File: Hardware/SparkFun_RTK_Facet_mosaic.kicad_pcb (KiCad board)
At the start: 4 copper layers, 59.5 x 43 mm, 128 parts, among them J1 U.FL_SMD, J2 JST_2mm_LiPo, J3 Qwiic_RA, J5 Conn_01x12_FPC_0.5mm, J6 Conn_01x12_FPC_0.5mm, J7 Conn_01x12_FPC_0.5mm, Q1 MBT3904DW1, Q2 SIL2308, U1 ESP32-PICO-V3-02, U10 MCP73833_MSOP, U11 AP2112K-3.3, U12 STLQ015-3.3, U13 74HC4052D, U2 mosaic-X5, U3 CH340C, U4 MAX17048, U5 AP2112K-3.3, U6 Power_Divider, U8 NEO-D9S, U9 USB251xB, Y1 24MHz

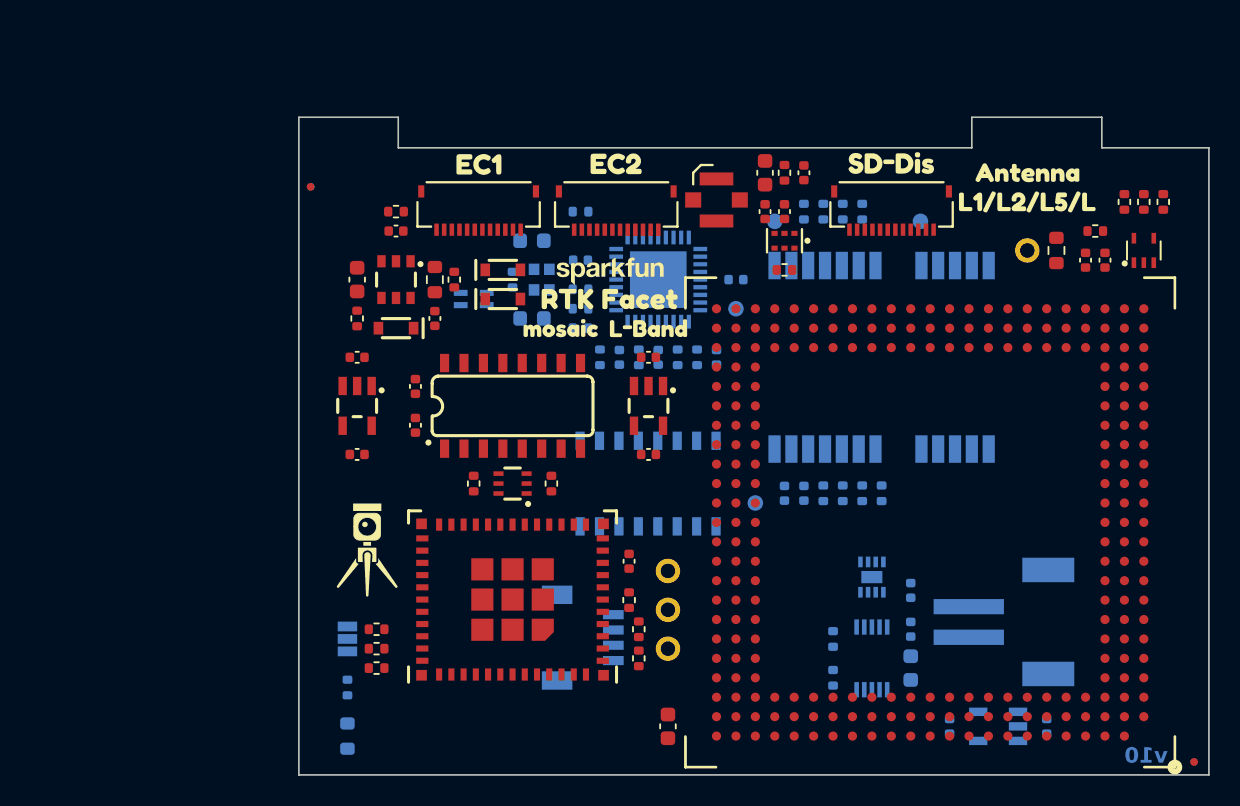
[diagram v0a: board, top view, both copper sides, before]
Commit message: Schematic updates
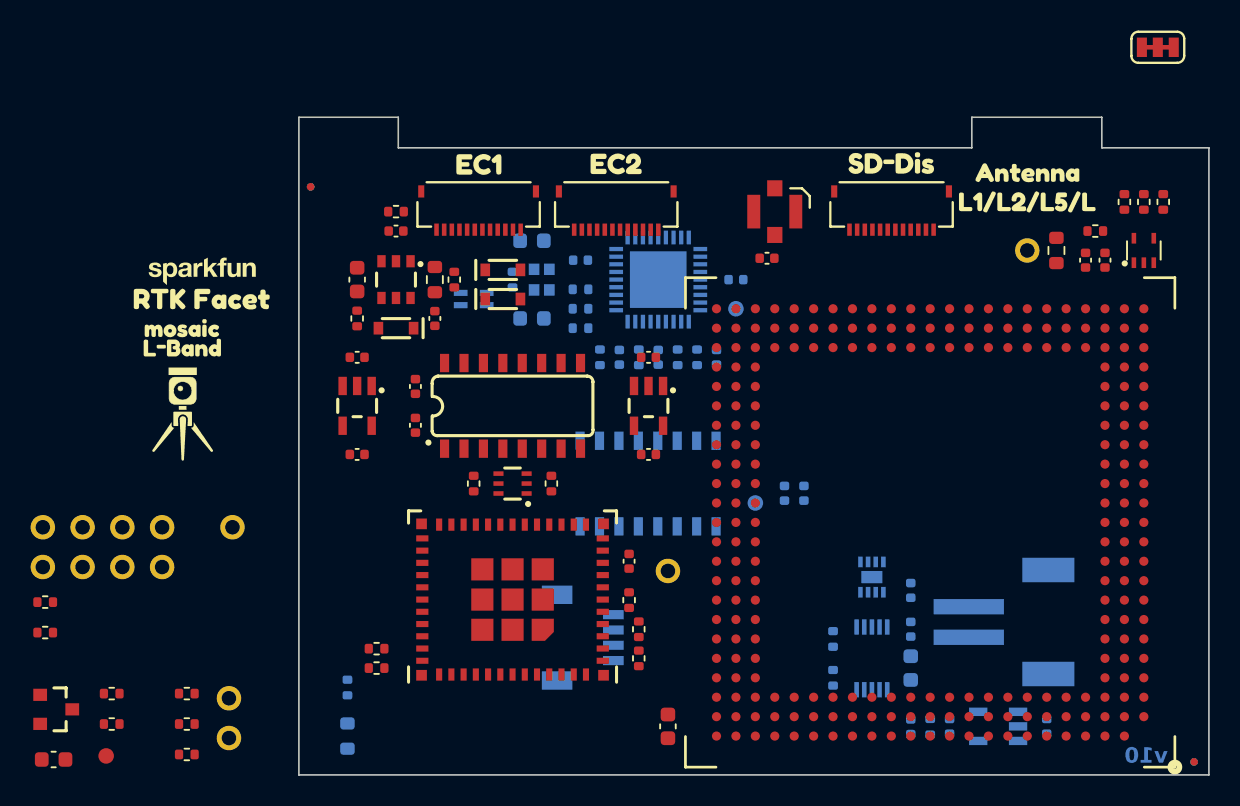
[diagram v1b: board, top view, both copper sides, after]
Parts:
- removed C9: 47pF, SparkFun-Capacitor:C_0402_1005Metric
- removed R18: 33, SparkFun-Resistor:R_0402_1005Metric
- removed R22: 100k, SparkFun-Resistor:R_0402_1005Metric
- removed R39, R40: 27, SparkFun-Resistor:R_0402_1005Metric
- removed U6: Power_Divider, SparkFun-RF:PD0922J5050S2HF_ANA
- removed U8: NEO-D9S, SparkFun-GPS:NEO-M9N_M8T_M8U_D9S_F9P_F10N
- added Q3: BSS138, SparkFun-Semiconductor-Standard:SOT23-3, F.Cu at (85.7, 148.1)
- added TP10: PTH, SparkFun-Connector:1X01, F.Cu at (90.1, 138.8)
- added TP11: PTH, SparkFun-Connector:1X01, F.Cu at (92.7, 136.2)
- added TP12: PTH, SparkFun-Connector:1X01, F.Cu at (92.7, 138.8)
- added TP13: PTH, SparkFun-Connector:1X01, F.Cu at (97.3, 136.2)
- added TP14: 1.0mm, SparkFun-Connector:TestPoint-1.0mm, F.Cu at (89.0, 151.2)
- added TP15: PTH, SparkFun-Connector:1X01, F.Cu at (97.0, 147.4)
- added TP16: PTH, SparkFun-Connector:1X01, F.Cu at (97.0, 150.0)
- added TP9: PTH, SparkFun-Connector:1X01, F.Cu at (90.1, 136.2)
- C3: value 47pF -> 0.1uF; moved to B.Cu
- JP1: footprint SparkFun-Jumper:SMT-JUMPER_3_NO_SILK -> SparkFun-Jumper:SMT-JUMPER_3_2-NC_TRACE_SILK; moved to F.Cu
- L1: value 2.66Ohm -> 470Ohm
- R10, R9: value 33 -> 10k; moved to F.Cu
- R11: value 10 -> 10k; moved to B.Cu
- R12: value 100 -> 2.2k
- R13: value 33 -> 2.2k; moved to F.Cu
- R14, R15: value 33 -> 100k; moved to F.Cu
- R17: value 10k -> 12k
- TP1, TP4: value 1.0mm -> PTH; footprint SparkFun-Connector:TestPoint-1.0mm -> SparkFun-Connector:1X01; moved to F.Cu
- moved JP1 65.6 mm to (157.8, 104.8), turned to 0 degrees
- moved TP1 60.8 mm to (84.9, 136.2), turned to 0 degrees
- moved L1 60.3 mm to (85.6, 151.4), turned to 0 degrees
- moved R13 56.3 mm to (89.4, 149.1), turned to 0 degrees
- moved R9 55.1 mm to (85.0, 141.1), turned to 0 degrees
- moved R10 54.2 mm to (85.0, 143.1), turned to 0 degrees
- moved TP4 52.9 mm to (84.9, 138.8)
- moved R14 52.2 mm to (94.3, 147.1), turned to 0 degrees
- moved R12 52.0 mm to (89.4, 147.1)
- moved R15 45.5 mm to (94.3, 149.1), turned to 0 degrees
- moved TP7 38.7 mm to (87.5, 136.2)
- moved TP8 38.6 mm to (87.5, 138.8)
- moved R11 37.5 mm to (142.9, 149.3)
- moved C3 36.9 mm to (141.6, 149.3), turned to 90 degrees
- moved kibuzzard-65777033 30.5 mm to (94.0, 124.5)
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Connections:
- C3 pad 1: Net-(C3-Pad1) -> Net-(U2-~{RESET})
- D1 pad 2: Net-(D1-A2) -> MOSAIC_RF_IN
- J1 pad 1: Net-(D1-A2) -> MOSAIC_RF_IN
- J2 pad NC1: (no net) -> unconnected-(J2-PadNC1)
- J2 pad NC2: (no net) -> unconnected-(J2-PadNC2)
- J3 pad 3: ESP8/SDA -> ESP21/SDA
- J3 pad 4: ESP9/SCL -> ESP22/SCL
- J6 pad 3: ESP9/SCL -> ESP22/SCL
- J6 pad 4: ESP8/SDA -> ESP21/SDA
- J7 pad 11: CHG_LED -> ESP34/CHG_LED
- JP1 pad 2: 3.3V_P -> 3.3V
- L1 pad 1: Net-(C3-Pad1) -> VRAW
- L1 pad 2: Net-(D1-A2) -> VANT
- R10 pad 1: Net-(U8-SCL/SCK) -> 3.3V
- R10 pad 2: ESP22/SCL -> ESP34/CHG_LED
- R11 pad 1: Net-(C3-Pad1) -> 3.3V_P
- R11 pad 2: 3.3V_P -> Net-(U2-~{RESET})
- R12 pad 1: MOSAIC_RF_IN -> 1.8V
- R12 pad 2: NEO_RF_IN -> MPPS
- R13 pad 1: Net-(U8-TX2) -> 3.3V_P
- R13 pad 2: ESP4/NEO_TX -> MPPS_3V3
- R14 pad 1: Net-(U8-RX2) -> Net-(U9-SDA)
- R14 pad 2: ESP25/NEO_RX -> GND
- R15 pad 1: Net-(U8-TX1/POCI) -> Net-(U9-SCL/CFG0)
- R15 pad 2: unconnected-(R15-Pad2) -> GND
- R17 pad 1: 3.3V_P -> GND
- R17 pad 2: ESP19/MLOG -> Net-(U9-RBIAS)
- R37 pad 2: SD_CLK -> SD_CMD
- R7 pad 2: ESP36/DeviceSense -> ESP35/DeviceSense
- R8 pad 1: ESP36/DeviceSense -> ESP35/DeviceSense
- R9 pad 1: Net-(U8-SDA/~{CS}) -> 3.3V
- R9 pad 2: ESP21/SDA -> ESP36/CHG_S2
- TP1 pad 1: Net-(U8-~{RESET}) -> 3.3V
- TP4 pad 1: Net-(U8-~{SAFEBOOT}) -> GND
- TP7 pad 1: 3.3V -> 3.3V_P
- TP8 pad 1: GND -> VRAW
- U1 pad 10: ESP35/CHG_S2 -> ESP35/DeviceSense
- U1 pad 15: ESP25/NEO_RX -> ESP25/MRX4
- U1 pad 21: ESP15/M~{RESET} -> unconnected-(U1-IOA15-Pad21)
- U1 pad 24: ESP4/NEO_TX -> ESP4/MTX4
- U1 pad 33: ESP19/MLOG -> unconnected-(U1-IO19-Pad33)
- U1 pad 4: ESP36/DeviceSense -> ESP36/CHG_S2
- U1 pad 5: unconnected-(U1-IA37-Pad5) -> ESP37/MRDY
- U10 pad 4: ESP35/CHG_S2 -> ESP36/CHG_S2
- U13 pad 14: MPPS -> MPPS_3V3
- U13 pad 15: ESP9/SCL -> ESP22/SCL
- U13 pad 2: ESP8/SDA -> ESP21/SDA
- U2 pad A11: ESP15/M~{RESET} -> Net-(U2-~{RESET})
- U2 pad A12: unconnected-(U2-MODULE_RDY-PadA12) -> ESP37/MRDY
- U2 pad A8: unconnected-(U2-V_USB-PadA8) -> VUSB
- U2 pad D1: ESP7/MTX2 -> ESP7/MTX1
- U2 pad D3: unconnected-(U2-COM4_RX-PadD3) -> ESP25/MRX4
- U2 pad E3: unconnected-(U2-COM4_TX-PadE3) -> ESP4/MTX4
- U2 pad K3: ESP19/MLOG -> unconnected-(U2-LOG_BTN-PadK3)
- U4 pad 9: (no net) -> GND
- U9 pad 22: unconnected-(U9-SDA-Pad22) -> Net-(U9-SDA)
- U9 pad 24: unconnected-(U9-SCL/CFG0-Pad24) -> Net-(U9-SCL/CFG0)
- U9 pad 6: NEO_DM -> unconnected-(U9-USBDM_DN3-Pad6)
- U9 pad 7: NEO_DP -> unconnected-(U9-USBDP_DN3-Pad7)

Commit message: Ready for airwire review
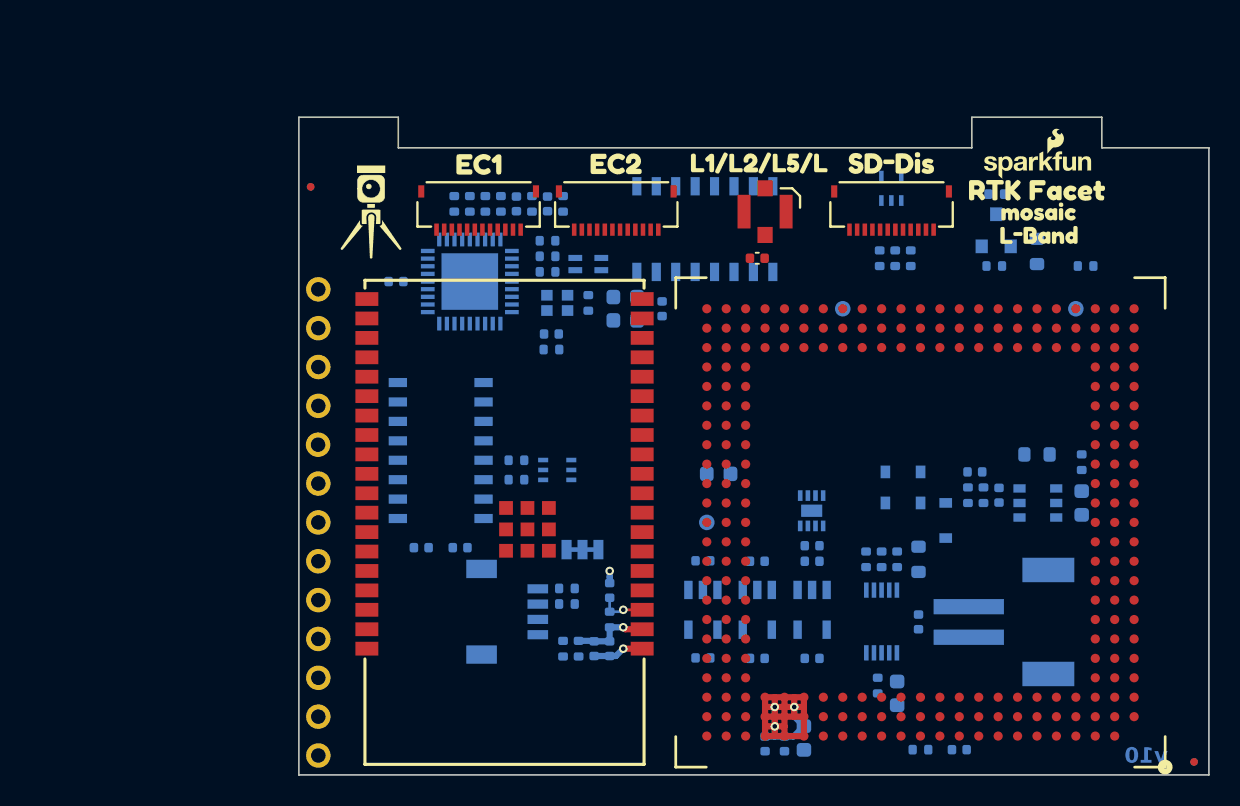
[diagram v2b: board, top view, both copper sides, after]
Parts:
- removed the G*** at (95.2, 119.4)
- removed R9: 10k, SparkFun-Resistor:R_0402_1005Metric
- removed kibuzzard-65776CD3: G***, kibuzzard-65776CD3
- added G***: LOGO, SparkFun-Aesthetic:SparkFun_Logo_7mm, F.Cu at (149.9, 112.4)
- C1, C18, C19, C2, C20, C21, C22, C23, C29, C4, C5, C7, C8, D2, D3, D4, D5, JP1, L1, Q1, Q2, Q3, R1, R10, R12, R13, R14, R15, R16, R17, R2, R28, R3, R33, R34, R35, R36, R37, R38, R4, R5, R6, R7, R8, TP14, U11, U3, U5: moved to B.Cu
- U1: value ESP32-PICO-V3-02 -> ESP32-WROVER-E-N16R8; footprint SparkFun-RF:ESP32-PICO-MINI -> SparkFun-RF:ESP32-WROVER-E-IE
- moved TP14 69.8 mm to (152.4, 121.9), turned to 180 degrees
- moved Q3 69.0 mm to (147.2, 116.8), turned to 90 degrees
- moved R13 67.4 mm to (147.2, 114.4), turned to 180 degrees
- moved R12 64.1 mm to (147.1, 119.1), turned to 180 degrees
- moved kibuzzard-65777037 56.5 mm to (150.0, 115.6)
- moved kibuzzard-65777033 56.5 mm to (150.0, 117.1)
- moved kibuzzard-65776CFF 55.1 mm to (149.9, 114.2)
- moved R10 54.5 mm to (139.4, 146.6), turned to 90 degrees
- moved G*** 51.8 mm to (143.5, 124.2)
- moved kibuzzard-65776CFF 51.1 mm to (143.4, 126.4)
- moved kibuzzard-65776D09 51.0 mm to (143.6, 128.0)
- moved kibuzzard-65776D0F 50.9 mm to (143.8, 129.8)
- moved JP1 49.9 mm to (120.1, 137.7)
- moved Ref** 49.9 mm to (106.3, 115.6)
- moved C20 49.6 mm to (152.8, 134.6), turned to -90 degrees
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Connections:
- D2 pad 1: SD_DATA -> Net-(D2-K1)
- D2 pad 3: SD_CLK -> SD_DATA
- D2 pad 4: SD_CMD -> SD_CLK
- D2 pad 5: Net-(D2-K4) -> SD_CMD
- J7 pad 5: Net-(D2-K4) -> Net-(D2-K1)
- Q1 pad 6: ESP0/STAT -> ESP0/BOOT
- R28 pad 2: Net-(D2-K4) -> Net-(D2-K1)
- TP6 pad 1: MPPS -> MPPS_3V3
- U1 pad 10: ESP35/DeviceSense -> ESP25/MRX4
- U1 pad 11: GND -> ESP26/DAC2
- U1 pad 12: ESP32/PowerControl -> ESP27/PeripheralPower
- U1 pad 13: ESP33/FastOff -> ESP14/MRX1
- U1 pad 14: GND -> unconnected-(U1-IOA12-Pad14)
- U1 pad 15: ESP25/MRX4 -> GND
- U1 pad 16: ESP26/DAC2 -> ESP13/MTX1
- U1 pad 17: ESP27/PeripheralPower -> unconnected-(U1-NC-Pad17)
- U1 pad 18: ESP14/MUXB -> unconnected-(U1-NC-Pad18)
- U1 pad 2: GND -> 3.3V
- U1 pad 20: ESP13/MUXA -> unconnected-(U1-NC-Pad20)
- U1 pad 23: ESP0/STAT -> unconnected-(U1-IOA15-Pad23)
- U1 pad 24: ESP4/MTX4 -> unconnected-(U1-IOA2-Pad24)
- U1 pad 25: unconnected-(U1-NC-Pad25) -> ESP0/BOOT
- U1 pad 26: ESP20/MOnOff -> ESP4/MTX4
- U1 pad 27: ESP7/MTX1 -> unconnected-(U1-NC-Pad27)
- U1 pad 28: ESP8/MRX1 -> unconnected-(U1-NC-Pad28)
- U1 pad 3: 3.3V -> ESP~{RST}
- U1 pad 30: ESP3/CH340-TX -> ESP18/MUXA
- U1 pad 31: ESP1/CH340-RX -> ESP19/MUXB
- U1 pad 33: unconnected-(U1-IO19-Pad33) -> ESP21/SDA
- U1 pad 34: ESP22/SCL -> ESP3/CH340-TX
- U1 pad 35: ESP21/SDA -> ESP1/CH340-RX
- U1 pad 36: GND -> ESP22/SCL
- U1 pad 37: GND -> ESP23/MOnOff
- U1 pad 4: ESP36/CHG_S2 -> ESP36/MRDY
- U1 pad 5: ESP37/MRDY -> ESP39/ADC39
- U1 pad 6: unconnected-(U1-IA38-Pad6) -> ESP34/CHG_LED
- U1 pad 7: ESP39/ADC39 -> ESP35/DeviceSense
- U1 pad 8: ESP~{RST} -> ESP32/PowerControl
- U1 pad 9: ESP34/CHG_LED -> ESP33/FastOff
- U10 pad 4: ESP36/CHG_S2 -> unconnected-(U10-STAT2-Pad4)
- U13 pad 10: ESP13/MUXA -> ESP18/MUXA
- U13 pad 9: ESP14/MUXB -> ESP19/MUXB
- U2 pad A10: ESP20/MOnOff -> ESP23/MOnOff
- U2 pad A12: ESP37/MRDY -> ESP36/MRDY
- U2 pad B1: ESP8/MRX1 -> ESP14/MRX1
- U2 pad D1: ESP7/MTX1 -> ESP13/MTX1
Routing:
- net 3.3V_P: track 0.00 -> 29.1 mm, vias 0 -> 3
- net 3.3V: track 0.00 -> 5.27 mm, vias 0 -> 1
- net GND: track 0.00 -> 4.13 mm, vias 0 -> 2
- net ESP~{RST}: track 0.00 -> 3.09 mm, vias 0 -> 1
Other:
- board text added: "N.Seidle and P.Clark"
- board text removed: "N.Seidle"

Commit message: Work in progress...
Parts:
- added TP17: 1.0mm, SparkFun-Connector:TestPoint-1.0mm, B.Cu at (121.9, 133.3)
- added TP18: 1.0mm, SparkFun-Connector:TestPoint-1.0mm, B.Cu at (121.9, 128.3)
- TP15, TP16: value PTH -> 1.0mm; footprint SparkFun-Connector:1X01 -> SparkFun-Connector:TestPoint-1.0mm; moved to B.Cu
- TR1: value RFCMF1220100M4T -> Val**
- moved Ref** 49.9 mm to (156.2, 116.3)
- moved Ref** 30.8 mm to (134.6, 127.6)
- moved TP15 19.7 mm to (121.9, 125.7), turned to 180 degrees
- moved TP16 19.2 mm to (121.9, 130.8), turned to 180 degrees
- moved TP1 10.2 mm to (102.9, 135.9)
- moved TP11 10.2 mm to (102.9, 128.3)
- moved TP12 10.2 mm to (102.9, 130.8)
- moved TP7 10.2 mm to (102.9, 138.4)
- moved TP8 10.2 mm to (102.9, 133.3)
- moved TP9 10.2 mm to (102.9, 141.0)
- moved TP10 7.62 mm to (102.9, 143.5)
- moved TP4 7.62 mm to (102.9, 118.1)
- moved TP13 7.62 mm to (102.9, 125.7)
- moved R10 0.81 mm to (138.8, 146.1), turned to 0 degrees
- moved kibuzzard-65776D0F 0.57 mm to (143.5, 130.3)
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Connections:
- TP15 pad 1: ESP_DM -> ESP13/MTX1
- TP16 pad 1: ESP_DP -> ESP14/MRX1
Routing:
- net VUSB: track 0.00 -> 166.6 mm, vias 0 -> 7
- net 3.3V_P: track 29.1 -> 193.6 mm, vias 3 -> 13
- net 3.3V: track 5.27 -> 118.6 mm, vias 1 -> 15
- net VRAW: track 0.00 -> 108.7 mm, vias 0 -> 3
- net VIN: track 0.00 -> 89.0 mm, vias 0 -> 2
- net VBATT: track 0.00 -> 62.9 mm, vias 0 -> 2
- net M_BACKUP: track 0.00 -> 59.1 mm, vias 0 -> 1
- net GND: track 4.13 -> 57.5 mm, vias 2 -> 74
- net POWER_BTN: track 0.00 -> 52.0 mm, vias 0 -> 1
- net ESP32/PowerControl: track 0.00 -> 35.2 mm, vias 0 -> 3
- net ESP~{RST}: track 3.09 -> 37.6 mm, vias 1 -> 4
- net MPPS_3V3: track 0.00 -> 32.8 mm
- net CH340-~{RTS}: track 0.00 -> 15.0 mm, vias 0 -> 2
- net ESP0/BOOT: track 0.00 -> 15.0 mm, vias 0 -> 1
- net ESP21/SDA: track 0.00 -> 14.0 mm, vias 0 -> 1
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- added copper zone on B.Cu, net GND
- added copper zone on F.Cu, net GND
- added copper zone on In1.Cu, net GND

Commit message: Routed
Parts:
- added TP19: 1.0mm, SparkFun-Connector:TestPoint-1.0mm, B.Cu at (119.4, 113.0)
- added TP20: 1.0mm, SparkFun-Connector:TestPoint-1.0mm, B.Cu at (121.9, 113.0)
- TR1: value Val** -> RFCMF1220100M4T
- moved R16 1.27 mm to (149.9, 116.8)
- moved D2 0.77 mm to (140.3, 113.8), turned to -90 degrees
- moved R37 0.65 mm to (140.6, 119.3)
- moved R38 0.65 mm to (139.6, 119.3)
- moved R28 0.65 mm to (141.6, 119.3)
- turned R13 to 180 degrees
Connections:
- D2 pad 1: Net-(D2-K1) -> SD_DATA
- D2 pad 3: SD_DATA -> Net-(D2-K2)
- D2 pad 4: SD_CLK -> SD_CMD
- D2 pad 5: SD_CMD -> SD_CLK
- J7 pad 5: Net-(D2-K1) -> Net-(D2-K2)
- R28 pad 2: Net-(D2-K1) -> Net-(D2-K2)
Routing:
- net MPPS_3V3: track 32.8 -> 108.8 mm, vias 0 -> 3
- net ESP21/SDA: track 14.0 -> 84.8 mm, vias 1 -> 8
- net ESP22/SCL: track 13.3 -> 84.0 mm, vias 1 -> 7
- net ESP4/MTX4: track 0.00 -> 68.9 mm, vias 0 -> 2
- net MOSAIC_DP: track 0.00 -> 61.5 mm, vias 0 -> 2
- net MOSAIC_DM: track 0.00 -> 59.9 mm, vias 0 -> 2
- net MRX2: track 0.00 -> 59.7 mm, vias 0 -> 2
- net MTX2: track 0.00 -> 58.5 mm, vias 0 -> 2
- net ESP13/MTX1: track 0.00 -> 54.5 mm, vias 0 -> 2
- net MRX3: track 0.00 -> 54.1 mm, vias 0 -> 2
- net ESP14/MRX1: track 0.00 -> 53.3 mm, vias 0 -> 3
- net ESP25/MRX4: track 0.00 -> 52.5 mm, vias 0 -> 3
- net MEventA: track 0.00 -> 52.1 mm, vias 0 -> 2
- net ESP34/CHG_LED: track 1.92 -> 50.3 mm, vias 0 -> 5
- net ESP23/MOnOff: track 0.00 -> 42.9 mm, vias 0 -> 2
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- added copper zone on In2.Cu, net GND
